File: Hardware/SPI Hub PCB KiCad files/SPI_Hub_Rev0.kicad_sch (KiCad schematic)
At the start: 28 parts, among them J1 Conn_01x06_Socket, J2 Left Front, J3 Left Center, J4 Left Rear, J5 Right Front, J6 Right Center, J7 Right Rear, J8 Conn_01x03_Socket, U1 74AHC595

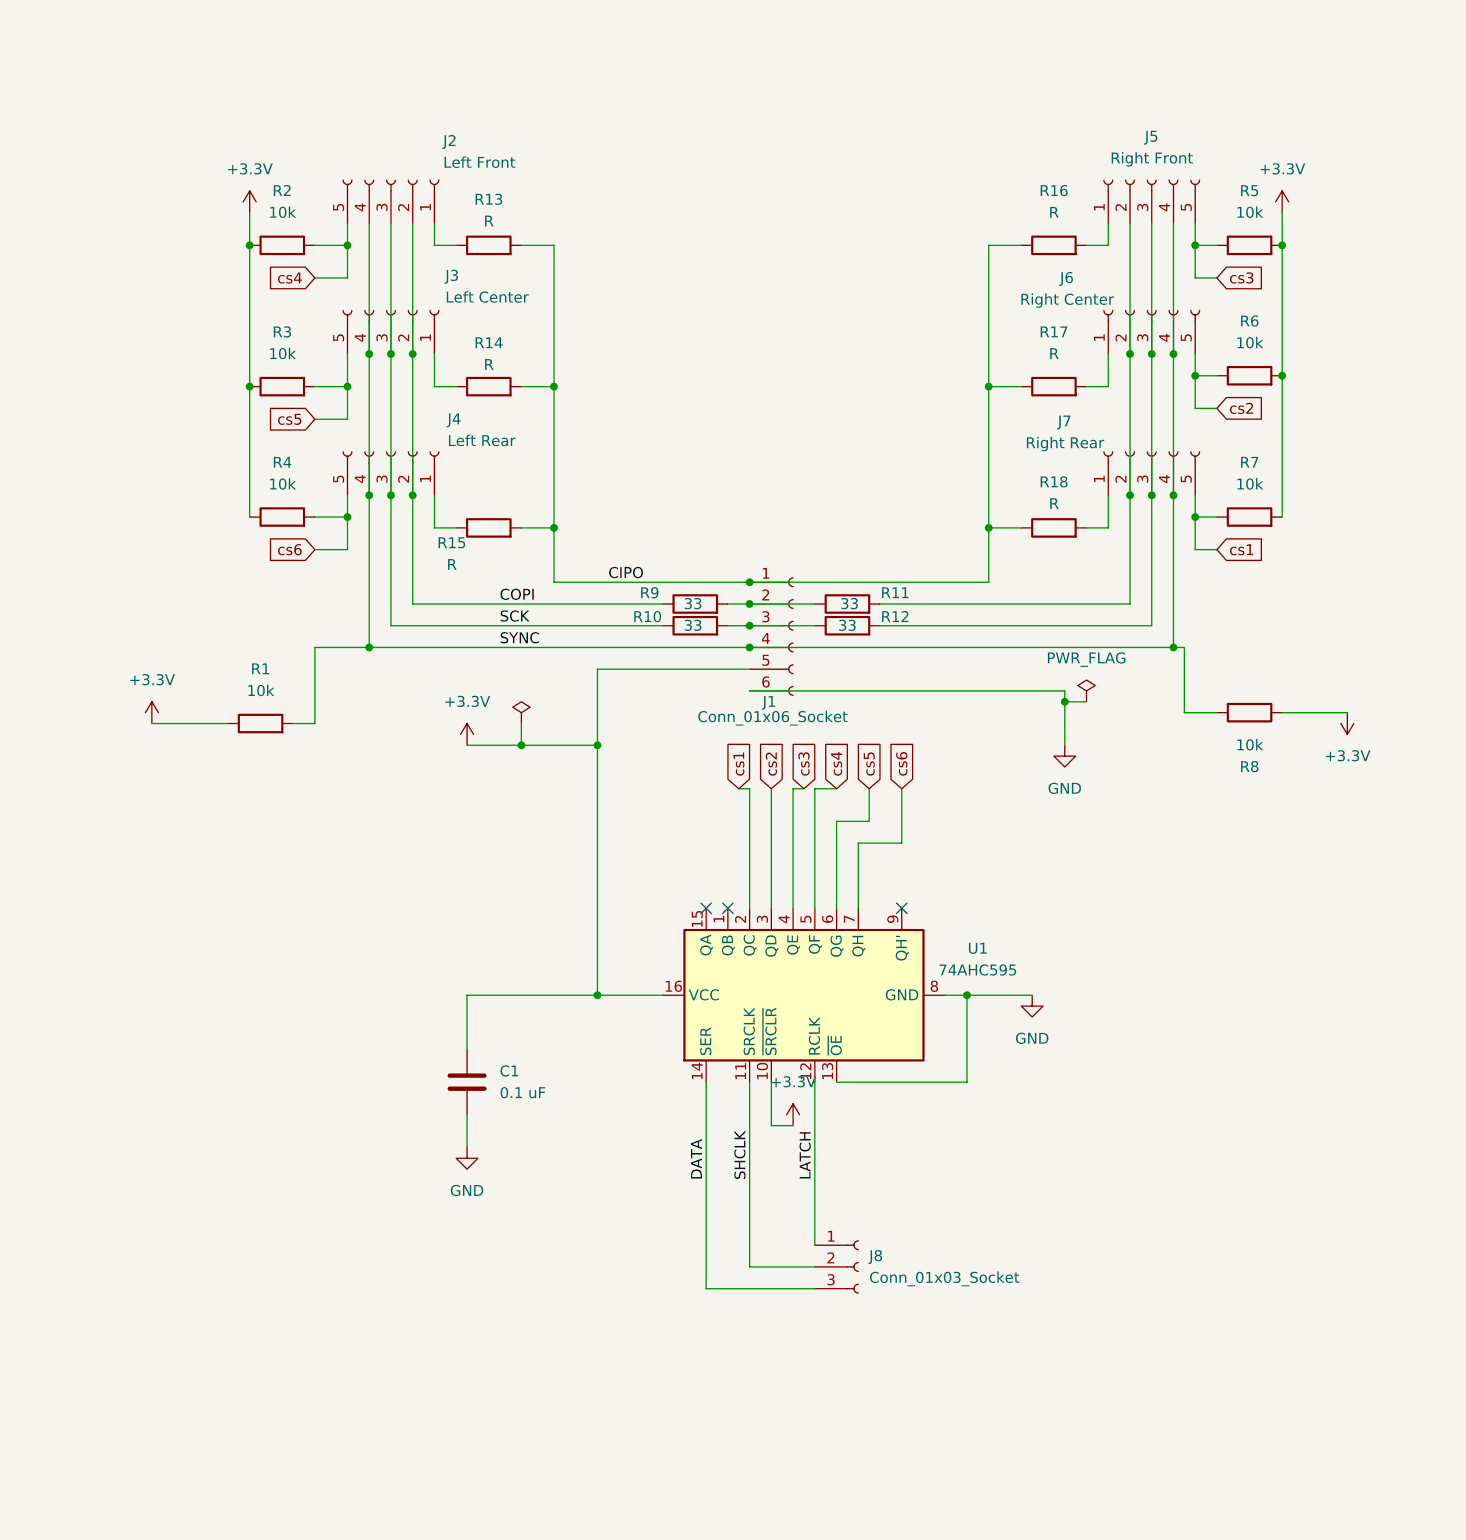
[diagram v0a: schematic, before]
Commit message: Updated and simplified PCB design
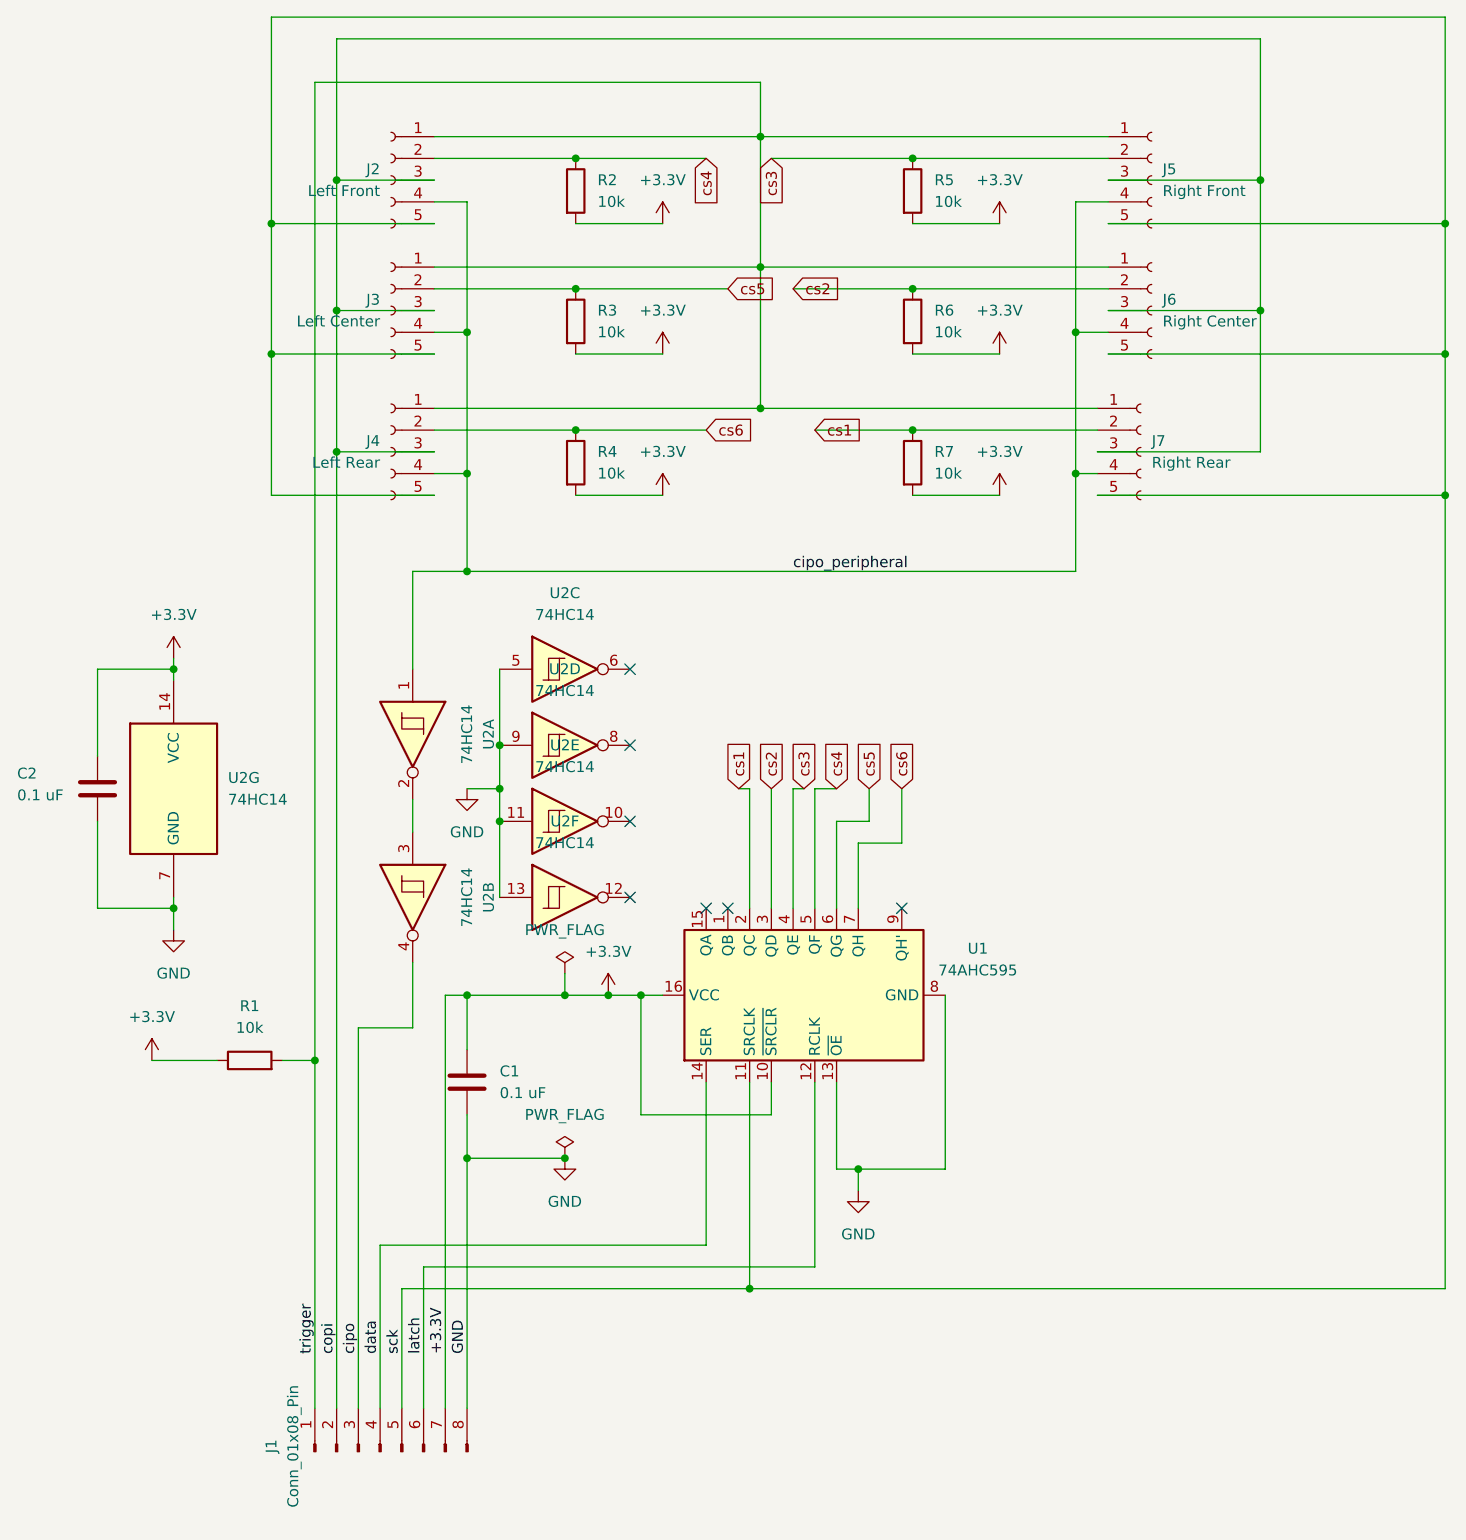
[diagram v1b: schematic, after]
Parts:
- removed J1: Conn_01x06_Socket, Connector_JST:JST_XH_B6B-XH-A_1x06_P2.50mm_Vertical, symbol Connector:Conn_01x06_Socket
- removed J8: Conn_01x03_Socket, Connector_JST:JST_XH_B3B-XH-A_1x03_P2.50mm_Vertical, symbol Connector:Conn_01x03_Socket
- removed R10, R11, R12, R9: 33, Resistor_SMD:R_0805_2012Metric_Pad1.20x1.40mm_HandSolder, symbol Device:R
- removed R13, R14, R15, R16, R17, R18: R, Resistor_SMD:R_0805_2012Metric_Pad1.20x1.40mm_HandSolder, symbol Device:R
- removed R8: 10k, Resistor_SMD:R_0805_2012Metric_Pad1.20x1.40mm_HandSolder, symbol Device:R
- added C2: 0.1 uF, Capacitor_SMD:C_0805_2012Metric_Pad1.18x1.45mm_HandSolder, symbol Device:C
- added J1: Conn_01x08_Pin, Connector_PinHeader_2.00mm:PinHeader_1x08_P2.00mm_Vertical, symbol Connector:Conn_01x08_Pin
- added U2: 74HC14, Package_SO:SOIC-14_3.9x8.7mm_P1.27mm, symbol 74xx:74HC14
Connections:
- net SCK is gone; now on net copi: J2.3 (Pin_3), J3.3 (Pin_3), J4.3 (Pin_3)
- net +3.3V: now also R2.2, R3.2, R4.2, C2.1, J1.7 (Pin_7), U2.14 (VCC); no longer R2.1, R3.1, R4.1
- net GND: now also C2.2, J1.8 (Pin_8), U2.11, U2.13, U2.5, U2.7 (GND), U2.9
- net cs1: now also J7.2 (Pin_2); no longer J7.5 (Pin_5)
- net cs2: now also J6.2 (Pin_2); no longer J6.5 (Pin_5)
- net cs3: now also J5.2 (Pin_2); no longer J5.5 (Pin_5)
- net cs4: now also J2.2 (Pin_2), R2.1; no longer J2.5 (Pin_5), R2.2
- net cs5: now also J3.2 (Pin_2), R3.1; no longer J3.5 (Pin_5), R3.2
- net cs6: now also J4.2 (Pin_2), R4.1; no longer J4.5 (Pin_5), R4.2
- net trigger: now reaches J3.1 (Pin_1)
- net trigger: now also J2.1 (Pin_1), J4.1 (Pin_1), J5.1 (Pin_1), J6.1 (Pin_1), J7.1 (Pin_1), R1.2, J1.1 (Pin_1)
- net copi: now reaches J5.3 (Pin_3), J6.3 (Pin_3), J7.3 (Pin_3)
- net copi: now also J1.2 (Pin_2)
- removed net COPI: J2.2 (Pin_2), J3.2 (Pin_2), J4.2 (Pin_2)
- net DATA renamed data
- net data: now also J1.4 (Pin_4)
- net LATCH renamed latch
- net latch: now also J1.6 (Pin_6)
- net SHCLK renamed sck
- net sck: now also J2.5 (Pin_5), J3.5 (Pin_5), J4.5 (Pin_5), J5.5 (Pin_5), J6.5 (Pin_5), J7.5 (Pin_5), J1.5 (Pin_5)
- net SYNC renamed cipo_peripheral
- net cipo_peripheral: now also U2.1; no longer R1.2
- new net: U2.2, U2.3
- new net cipo: J1.3 (Pin_3), U2.4
- no-connect marks 3 -> 7
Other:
- moved on the sheet: J2, J3, J4, J5, J6, J7, R1, R2, R3, R4, R5, R6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
